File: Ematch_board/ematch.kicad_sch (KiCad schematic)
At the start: 56 parts, among them J1 Conn_01x02_Male, J2 Conn_01x02_Male, J3 Conn_01x02_Male, J4 Conn_01x02_Male, J5 Conn_01x02_Male, J6 Conn_01x02_Male, Q51 PMV20ENR, Q52 PMV20ENR, Q53 PMV20ENR, Q54 PMV20ENR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

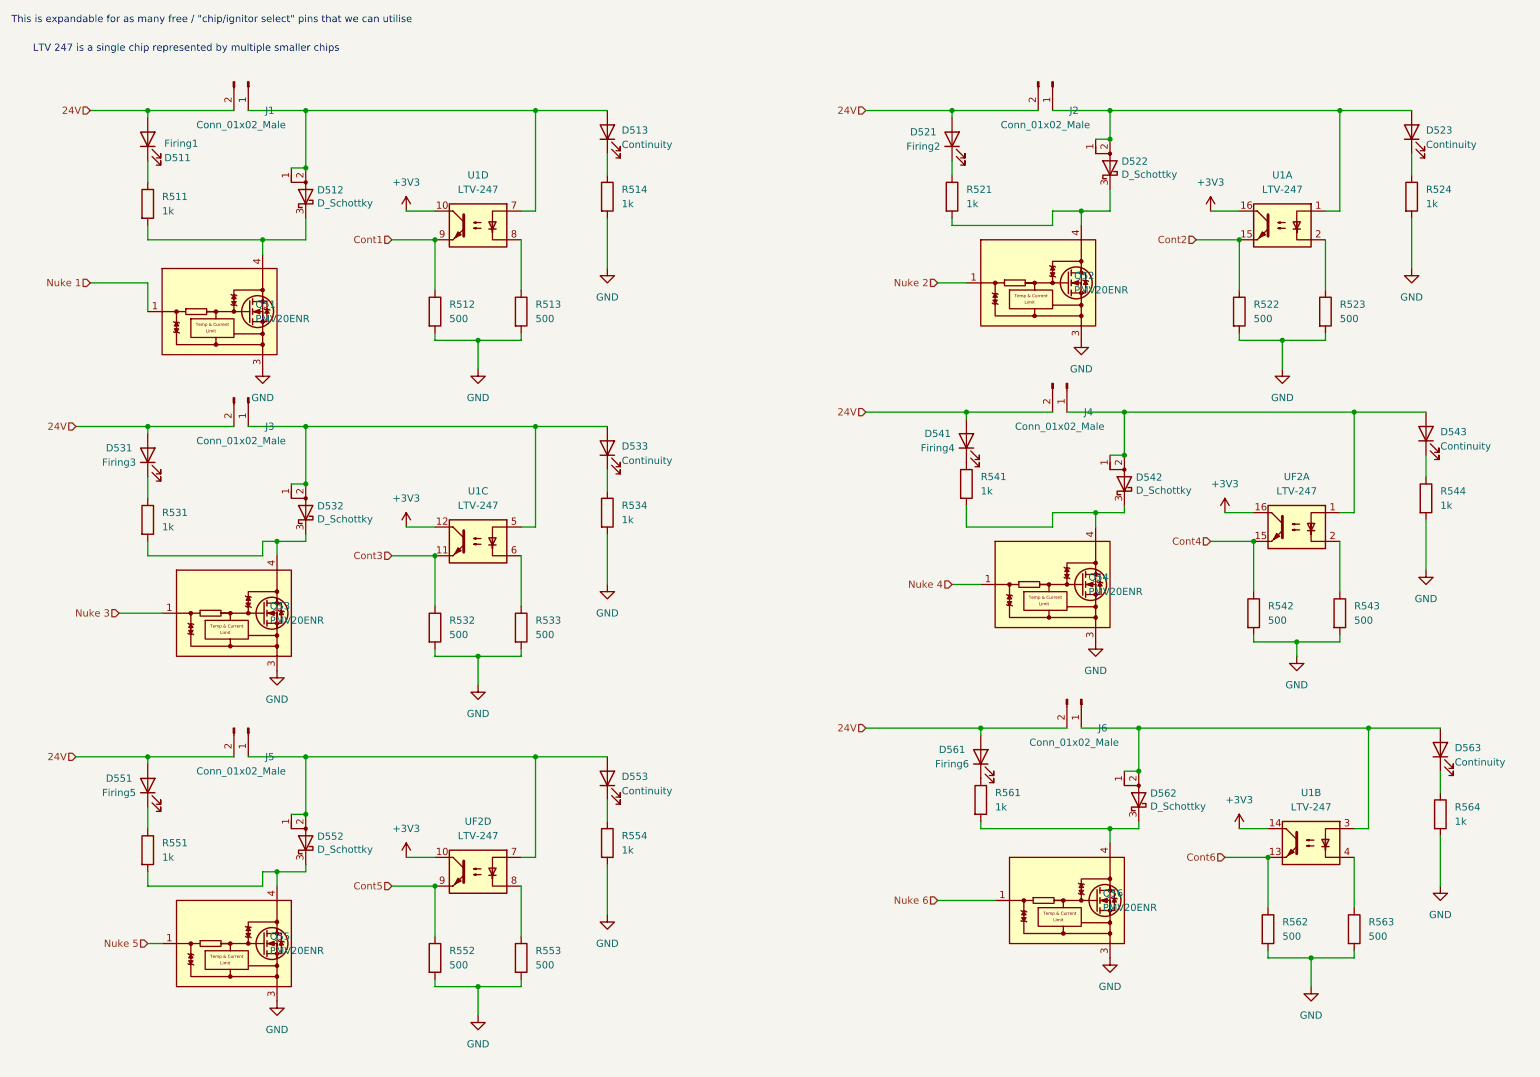
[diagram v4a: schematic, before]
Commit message: fixed unroute nets and changed LED resistor values
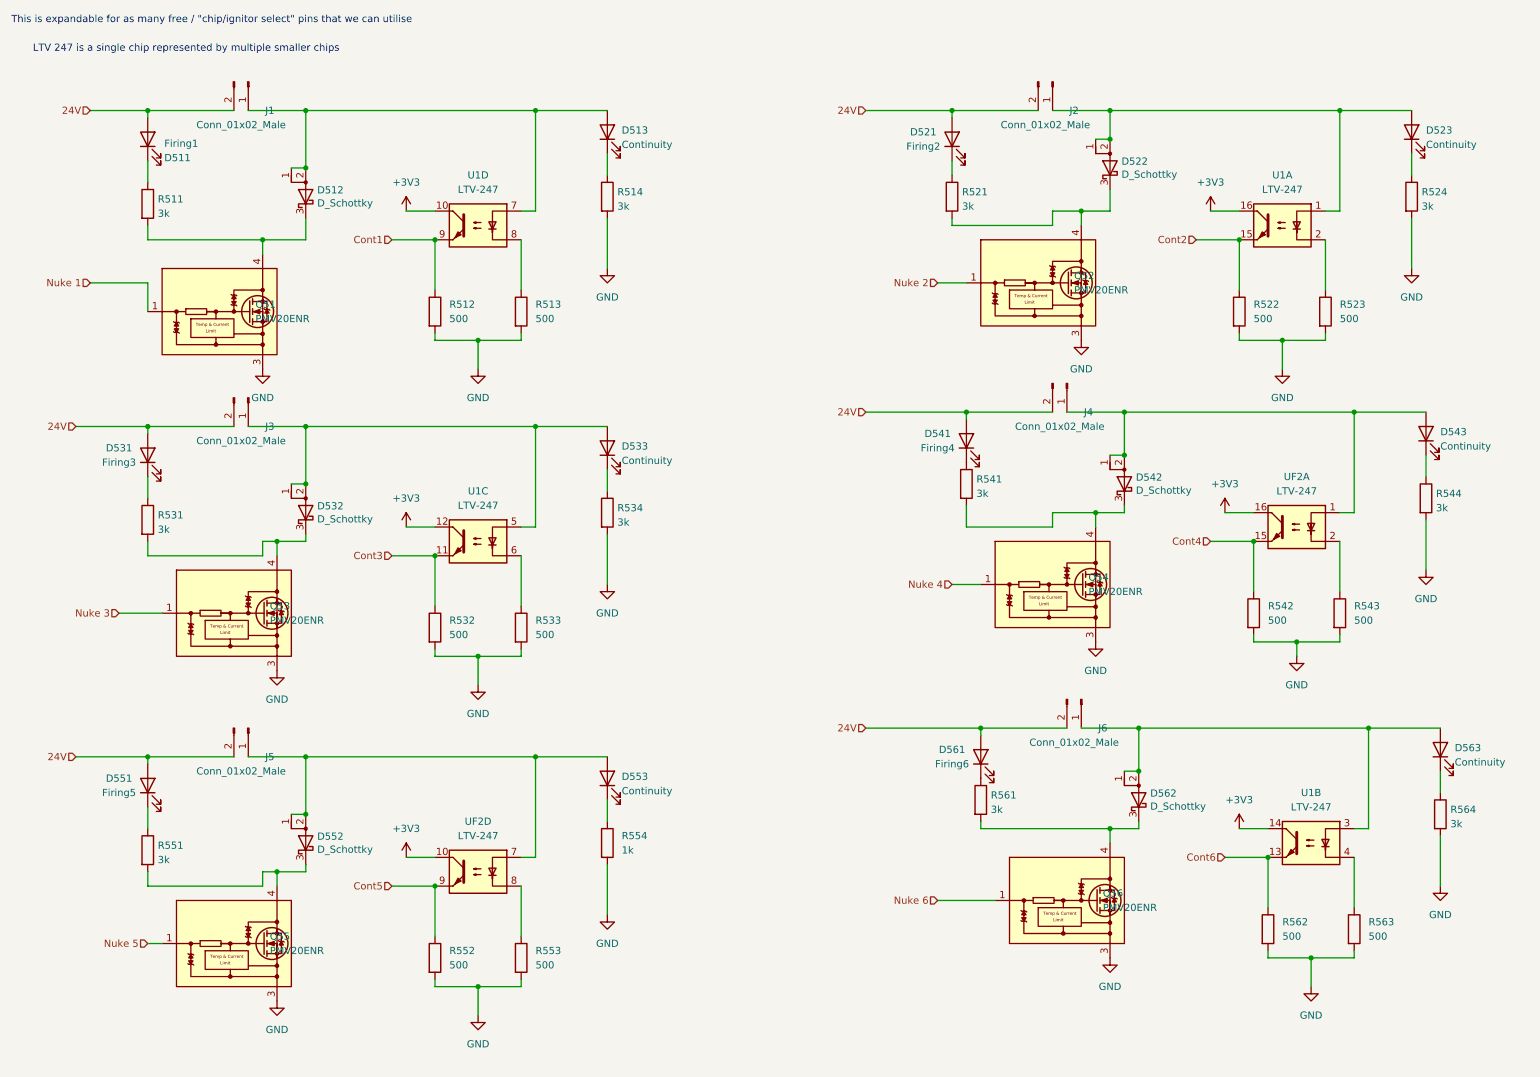
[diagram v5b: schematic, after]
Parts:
- R511, R514, R521, R524, R531, R534, R541, R544, R551, R561, R564: value 1k -> 3k
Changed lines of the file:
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@@
   (symbol (lib_id "Device:R") (at 119.38 45.72 0) (unit 1)
     (in_bom yes) (on_board yes) (fields_autoplaced)
-    (property "Reference" "R514" (id 0) (at 121.92 44.4499 0)
-      (effects (font (size 1.27 1.27)) (justify left))
-    )
-    (property "Value" "1k" (id 1) (at 121.92 46.9899 0)
+    (property "Reference" "R514" (id 0) (at 121.158 44.8853 0)
+      (effects (font (size 1.27 1.27)) (justify left))
+    )
+    (property "Value" "3k" (id 1) (at 121.158 47.4222 0)
       (effects (font (size 1.27 1.27)) (justify left))
     )
@@
   (symbol (lib_id "Device:R") (at 38.1 161.29 0) (unit 1)
     (in_bom yes) (on_board yes) (fields_autoplaced)
-    (property "Reference" "R551" (id 0) (at 40.64 160.0199 0)
-      (effects (font (size 1.27 1.27)) (justify left))
-    )
-    (property "Value" "1k" (id 1) (at 40.64 162.5599 0)
+    (property "Reference" "R551" (id 0) (at 39.878 160.4553 0)
+      (effects (font (size 1.27 1.27)) (justify left))
+    )
+    (property "Value" "3k" (id 1) (at 39.878 162.9922 0)
       (effects (font (size 1.27 1.27)) (justify left))
     )
@@
   (symbol (lib_id "Device:R") (at 180.34 45.72 0) (unit 1)
     (in_bom yes) (on_board yes) (fields_autoplaced)
-    (property "Reference" "R521" (id 0) (at 182.88 44.4499 0)
-      (effects (font (size 1.27 1.27)) (justify left))
-    )
-    (property "Value" "1k" (id 1) (at 182.88 46.9899 0)
+    (property "Reference" "R521" (id 0) (at 182.118 44.8853 0)
+      (effects (font (size 1.27 1.27)) (justify left))
+    )
+    (property "Value" "3k" (id 1) (at 182.118 47.4222 0)
       (effects (font (size 1.27 1.27)) (justify left))
     )
@@
   (symbol (lib_id "Device:R") (at 119.38 101.6 0) (unit 1)
     (in_bom yes) (on_board yes) (fields_autoplaced)
-    (property "Reference" "R534" (id 0) (at 121.92 100.3299 0)
-      (effects (font (size 1.27 1.27)) (justify left))
-    )
-    (property "Value" "1k" (id 1) (at 121.92 102.8699 0)
+    (property "Reference" "R534" (id 0) (at 121.158 100.7653 0)
+      (effects (font (size 1.27 1.27)) (justify left))
+    )
+    (property "Value" "3k" (id 1) (at 121.158 103.3022 0)
       (effects (font (size 1.27 1.27)) (justify left))
     )
@@
   (symbol (lib_id "Device:R") (at 182.88 96.52 0) (unit 1)
     (in_bom yes) (on_board yes) (fields_autoplaced)
-    (property "Reference" "R541" (id 0) (at 185.42 95.2499 0)
-      (effects (font (size 1.27 1.27)) (justify left))
-    )
-    (property "Value" "1k" (id 1) (at 185.42 97.7899 0)
+    (property "Reference" "R541" (id 0) (at 184.658 95.6853 0)
+      (effects (font (size 1.27 1.27)) (justify left))
+    )
+    (property "Value" "3k" (id 1) (at 184.658 98.2222 0)
       (effects (font (size 1.27 1.27)) (justify left))
     )
@@
   (symbol (lib_id "Device:R") (at 266.7 154.94 0) (unit 1)
     (in_bom yes) (on_board yes) (fields_autoplaced)
-    (property "Reference" "R564" (id 0) (at 269.24 153.6699 0)
-      (effects (font (size 1.27 1.27)) (justify left))
-    )
-    (property "Value" "1k" (id 1) (at 269.24 156.2099 0)
+    (property "Reference" "R564" (id 0) (at 268.478 154.1053 0)
+      (effects (font (size 1.27 1.27)) (justify left))
+    )
+    (property "Value" "3k" (id 1) (at 268.478 156.6422 0)
       (effects (font (size 1.27 1.27)) (justify left))
     )
@@
   (symbol (lib_id "Device:R") (at 261.62 45.72 0) (unit 1)
     (in_bom yes) (on_board yes) (fields_autoplaced)
-    (property "Reference" "R524" (id 0) (at 264.16 44.4499 0)
-      (effects (font (size 1.27 1.27)) (justify left))
-    )
-    (property "Value" "1k" (id 1) (at 264.16 46.9899 0)
+    (property "Reference" "R524" (id 0) (at 263.398 44.8853 0)
+      (effects (font (size 1.27 1.27)) (justify left))
+    )
+    (property "Value" "3k" (id 1) (at 263.398 47.4222 0)
       (effects (font (size 1.27 1.27)) (justify left))
     )
@@
   (symbol (lib_id "Device:R") (at 38.1 46.99 0) (unit 1)
     (in_bom yes) (on_board yes) (fields_autoplaced)
-    (property "Reference" "R511" (id 0) (at 40.64 45.7199 0)
-      (effects (font (size 1.27 1.27)) (justify left))
-    )
-    (property "Value" "1k" (id 1) (at 40.64 48.2599 0)
+    (property "Reference" "R511" (id 0) (at 39.878 46.1553 0)
+      (effects (font (size 1.27 1.27)) (justify left))
+    )
+    (property "Value" "3k" (id 1) (at 39.878 48.6922 0)
       (effects (font (size 1.27 1.27)) (justify left))
     )
@@
   (symbol (lib_id "Device:R") (at 264.16 99.06 0) (unit 1)
     (in_bom yes) (on_board yes) (fields_autoplaced)
-    (property "Reference" "R544" (id 0) (at 266.7 97.7899 0)
-      (effects (font (size 1.27 1.27)) (justify left))
-    )
-    (property "Value" "1k" (id 1) (at 266.7 100.3299 0)
+    (property "Reference" "R544" (id 0) (at 265.938 98.2253 0)
+      (effects (font (size 1.27 1.27)) (justify left))
+    )
+    (property "Value" "3k" (id 1) (at 265.938 100.7622 0)
       (effects (font (size 1.27 1.27)) (justify left))
     )
@@
   (symbol (lib_id "Device:R") (at 38.1 102.87 0) (unit 1)
     (in_bom yes) (on_board yes) (fields_autoplaced)
-    (property "Reference" "R531" (id 0) (at 40.64 101.5999 0)
-      (effects (font (size 1.27 1.27)) (justify left))
-    )
-    (property "Value" "1k" (id 1) (at 40.64 104.1399 0)
+    (property "Reference" "R531" (id 0) (at 39.878 102.0353 0)
+      (effects (font (size 1.27 1.27)) (justify left))
+    )
+    (property "Value" "3k" (id 1) (at 39.878 104.5722 0)
       (effects (font (size 1.27 1.27)) (justify left))
     )
@@
   (symbol (lib_id "Device:R") (at 185.42 152.4 0) (unit 1)
     (in_bom yes) (on_board yes) (fields_autoplaced)
-    (property "Reference" "R561" (id 0) (at 187.96 151.1299 0)
-      (effects (font (size 1.27 1.27)) (justify left))
-    )
-    (property "Value" "1k" (id 1) (at 187.96 153.6699 0)
-      (effects (font (size 1.27 1.27)) (justify left))
-    )
+    (property "Reference" "R561" (id 0) (at 187.198 151.5653 0)
+      (effects (font (size 1.27 1.27)) (justify left))
+    )
+    (property "Value" "3k" (id 1) (at 187.198 154.1022 0)
+      (effects (font (size 1.27 1.27)) (justify left))
+    )

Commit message: forgot to stage this in the last commit
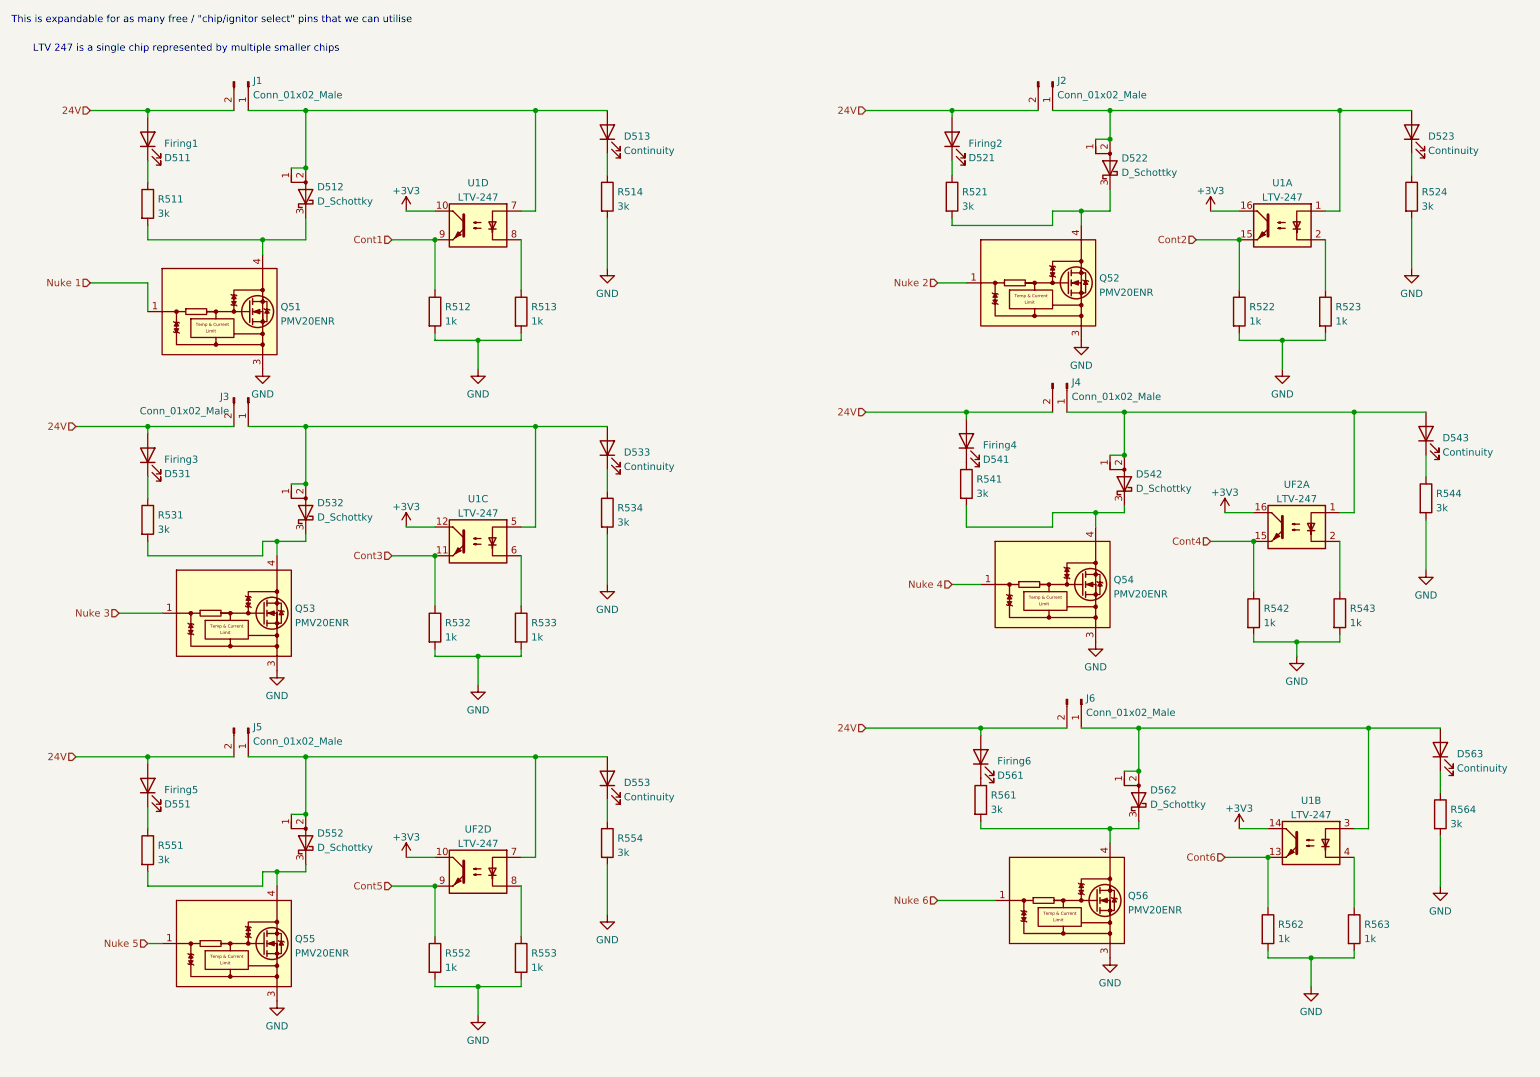
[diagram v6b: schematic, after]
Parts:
- R512, R513, R522, R523, R532, R533, R542, R543, R552, R553, R562, R563: value 500 -> 1k
- R554: value 1k -> 3k

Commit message: Changed ESP32 pin assignment from special IO pins
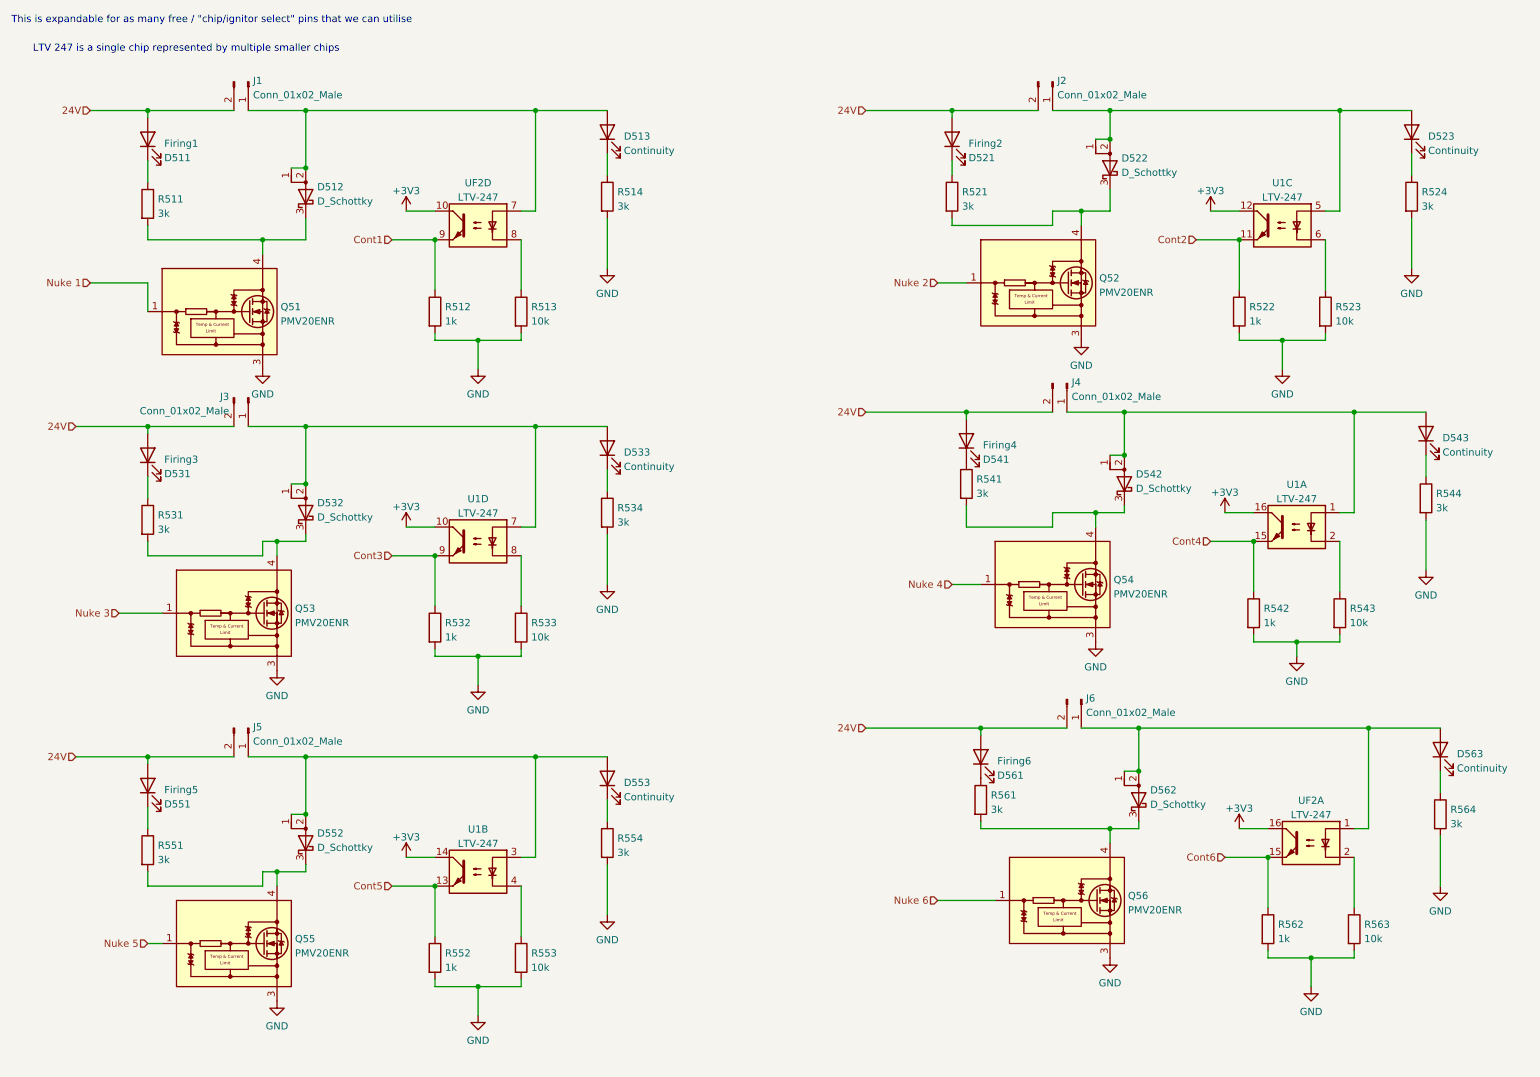
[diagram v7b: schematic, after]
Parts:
- removed unit 4 of UF2
- added unit 4 of U1
- R513, R523, R533, R543, R553, R563: value 1k -> 10k
- renumbered U1 to UF2
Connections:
- net +3V3: now also U1.10
- net Cont2: now also U1.11; no longer U1.15
- net Cont3: now also U1.9; no longer U1.11
- net Cont4: now also U1.15; no longer UF2.15
- net Cont5: now also U1.13
- net Cont6: now also UF2.15; no longer U1.13
- net at D522.1 (A), D522.2 (A), D523.2 (A)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: now also U1.5; no longer U1.1
- net at U1.2: now also R543.1; no longer R523.1
- net at D532.1 (A), D532.2 (A), D533.2 (A)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: now also U1.7; no longer U1.5
- net at R533.1: now also U1.8; no longer U1.6
- net at D542.1 (A), D542.2 (A), D543.2 (A)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: now also U1.1; no longer UF2.1
- net at R553.1: now also U1.4
- net at D552.1 (A), D552.2 (A), D553.2 (A)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: now also U1.3
- net at D562.1 (A), D562.2 (A), D563.2 (A)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: now also UF2.1; no longer U1.3
- net at R563.1: now also UF2.2; no longer U1.4
- new net: R523.1, U1.6
